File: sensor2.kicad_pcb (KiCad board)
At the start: 2 copper layers, 95 x 72 mm, 36 parts, among them CON1 DC2.5-9V, CON2 AVR-ISP-6, CON3 DM3AT-SF-PEJM5, IC1 ATMEGA328P-P, J1 AE-STEREO-MINI, P1 D-SUB9, P2 GMS6-CR6, P3 BATT, Q1 2SC1815, SW1 STOP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

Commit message: Developing
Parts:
- moved JP3 28.7 mm to (129.0, 129.0)
- moved CON3 26.0 mm to (104.0, 127.0)
- moved C3 25.8 mm to (117.1, 129.5)
- moved CON2 23.7 mm to (126.5, 136.4), turned to 0 degrees
- moved JP2 23.6 mm to (126.5, 129.0)
- moved J1 21.0 mm to (137.0, 133.0)
- moved JP1 18.6 mm to (124.0, 129.0)
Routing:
- net +3.3V: track 363.3 -> 265.4 mm
- net N-000005: track 92.3 -> 39.4 mm
- net N-000006: track 24.0 -> 0.00 mm
- net /3.3RX: track 11.6 -> 31.9 mm
- net /RX-LVTTL: track 55.8 -> 37.4 mm
- net /TX-LVTTL: track 50.8 -> 65.7 mm
- net N-0000022: track 2.54 -> 16.5 mm
- net N-000004: track 37.1 -> 26.2 mm
- net N-000003: track 40.5 -> 30.7 mm
- net GND: track 36.8 -> 27.1 mm
- net /3.3TX: track 13.7 -> 19.4 mm

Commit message: Critical miss
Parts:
- moved C3 16.1 mm to (101.0, 129.0)
- moved CON3 4.00 mm to (108.0, 127.0)
- moved R4 2.54 mm to (101.3, 111.0)
- moved P1 2.29 mm to (120.7, 108.0)
- moved P2 2.29 mm to (116.8, 111.0)
- moved CON2 2.18 mm to (125.2, 138.2), turned to 180 degrees
- moved R3 1.48 mm to (83.3, 111.3)
- moved R5 1.05 mm to (102.9, 108.2)
- moved R6 1.02 mm to (83.1, 106.9)
- moved CON1 1.00 mm to (68.0, 139.0)
- moved Q1 0.76 mm to (93.2, 106.9)
- moved U2 0.64 mm to (104.8, 119.4)
- moved SW1 0.51 mm to (134.6, 110.0)
- moved SW2 0.51 mm to (134.6, 118.1)
- moved C4 0.51 mm to (72.9, 106.4)
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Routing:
- net GND: track 27.1 -> 652.2 mm
- net +3.3V: track 265.4 -> 492.0 mm
- net N-000006: track 0.00 -> 108.9 mm
- net N-000004: track 26.2 -> 100.6 mm
- net N-000003: track 30.7 -> 99.6 mm, vias 0 -> 2
- net N-000002: track 0.00 -> 60.2 mm
- net /SDA: track 66.5 -> 121.4 mm
- net /SCL: track 69.2 -> 123.5 mm
- net N-0000022: track 16.5 -> 58.0 mm
- net N-000005: track 39.4 -> 0.00 mm
- net /3.3RX: track 31.9 -> 9.33 mm
- net +BATT: track 31.6 -> 49.3 mm
- net /TX-LVTTL: track 65.7 -> 82.7 mm
- net /RX-LVTTL: track 37.4 -> 33.9 mm
- net /TOGGLE: track 119.6 -> 121.8 mm
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- added copper zone on B.Cu, net GND
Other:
- net class Bold: via_dia 0.889 -> 1.524; via_drill 0.635 -> 1.016
- net class Default: via_dia 0.889 -> 1.524; via_drill 0.635 -> 1.016
- board text added: "JUMPER"

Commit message: First release
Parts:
- moved CON2 1.73 mm to (126.9, 137.7)
- moved R1 1.65 mm to (63.5, 126.6)
- moved R2 1.65 mm to (63.5, 129.2)
- moved R3 0.90 mm to (83.2, 110.4)
- moved R6 0.89 mm to (83.9, 106.9)
- moved JP1 0.76 mm to (124.7, 129.0)
- moved JP2 0.76 mm to (127.3, 129.0)
- moved JP3 0.76 mm to (129.8, 129.0)
- moved P2 0.38 mm to (116.8, 110.6)
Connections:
- CON1 pad 3: (no net) -> N-0000019
- P3 pad 2: GND -> N-0000019
- SW1 pad 3: (no net) -> GND
- SW2 pad 3: (no net) -> GND
- SW3 pad 4: (no net) -> GND
- SW4 pad 4: (no net) -> GND
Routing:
- net GND: track 652.2 -> 836.7 mm, vias 0 -> 4
- net N-000005: track 0.00 -> 63.9 mm, vias 0 -> 2
- net +3.3V: track 492.0 -> 532.8 mm
- net N-000006: track 99.6 -> 127.1 mm, vias 2 -> 4
- net N-0000019: track 0.00 -> 12.3 mm
- net +BATT: track 49.3 -> 39.7 mm
- net /SDA: track 121.4 -> 114.5 mm
- net /TOGGLE: track 121.8 -> 116.6 mm
- net /SCL: track 123.5 -> 119.8 mm
- net N-000007: track 108.9 -> 112.5 mm
- net /ADC0: track 33.0 -> 31.1 mm
- net N-000004: track 60.2 -> 58.7 mm
- net N-000001: track 100.6 -> 101.6 mm
- net N-000002: track 34.4 -> 35.2 mm
- net /3.3TX: track 18.8 -> 18.0 mm
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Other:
- board text added: "ISP"

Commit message: Developing
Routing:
- added copper zone on F.Cu, net GND
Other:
- net class Bold: via_dia 1.524 -> 0.889; via_drill 1.016 -> 0.635
- net class Default: via_dia 1.524 -> 0.889; via_drill 1.016 -> 0.635
- board text added: "Acc,Gyro"
- board text added: "Compass"
- board text added: "x"
- board text added: "y"
- board text added: "z"
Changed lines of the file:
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@@
-(kicad_pcb (version 3) (host pcbnew "(2013-07-07 BZR 4022)-stable")
+(kicad_pcb (version 3) (host pcbnew "(2013-jul-07)-stable")
   (general
     (links 97)
@@
     (area 32.57143 57.150001 152.2782 146.894321)
     (thickness 1.6)
-    (drawings 22)
+    (drawings 46)
     (tracks 676)
     (zones 0)
@@
     (last_trace_width 0.2032)
     (trace_clearance 0.2032)
-    (zone_clearance 0.4064)
+    (zone_clearance 0.508)
     (zone_45_only no)
     (trace_min 0.2032)
     (segment_width 0.2)
     (edge_width 0.1)
-    (via_size 1.524)
-    (via_drill 1.016)
+    (via_size 0.889)
+    (via_drill 0.635)
     (via_min_size 0.889)
     (via_min_drill 0.6096)
@@
     (visible_elements 7FFFFFFF)
     (pcbplotparams
-      (layerselection 283148289)
+      (layerselection 284196865)
       (usegerberextensions true)
       (excludeedgelayer true)
-      (linewidth 0.150000)
+      (linewidth 0.152400)
       (plotframeref false)
       (viasonmask true)
@@
     (clearance 0.2032)
     (trace_width 0.2032)
-    (via_dia 1.524)
-    (via_drill 1.016)
+    (via_dia 0.889)
+    (via_drill 0.635)
     (uvia_dia 0.508)
     (uvia_drill 0.127)
@@
     (clearance 0.2032)
     (trace_width 0.4064)
-    (via_dia 1.524)
-    (via_drill 1.016)
+    (via_dia 0.889)
+    (via_drill 0.635)
     (uvia_dia 0.508)
     (uvia_drill 0.127)
@@
     )
   )
+  (gr_text Compass (at 143.256 127.762) (layer F.SilkS)
+    (effects (font (size 1 1) (thickness 0.15)))
+  )
+  (gr_text z (at 140.716 125.984) (layer F.SilkS)
+    (effects (font (size 1.2 1.2) (thickness 0.15)))
+  )
+  (gr_text x (at 143.256 123.698) (layer F.SilkS)
+    (effects (font (size 1.2 1.2) (thickness 0.15)))
+  )
+  (gr_text y (at 144.78 125.984) (layer F.SilkS)
+    (effects (font (size 1.2 1.2) (thickness 0.15)))
+  )
+  (gr_circle (center 142.24 125.984) (end 142.748 126.492) (layer F.SilkS) (width 0.2))
+  (gr_line (start 142.748 126.492) (end 141.732 125.476) (angle 90) (layer F.SilkS) (width 0.2))
+  (gr_line (start 142.748 125.476) (end 141.732 126.492) (angle 90) (layer F.SilkS) (width 0.2))
+  (gr_line (start 144.018 125.984) (end 143.51 126.492) (angle 90) (layer F.SilkS) (width 0.2))
+  (gr_line (start 144.018 125.984) (end 143.51 125.476) (angle 90) (layer F.SilkS) (width 0.2))
+  (gr_line (start 142.24 124.206) (end 142.748 124.714) (angle 90) (layer F.SilkS) (width 0.2))
+  (gr_line (start 142.24 124.206) (end 141.732 124.714) (angle 90) (layer F.SilkS) (width 0.2))
+  (gr_line (start 142.24 125.984) (end 142.24 124.206) (angle 90) (layer F.SilkS) (width 0.2))
+  (gr_line (start 142.24 125.984) (end 144.018 125.984) (angle 90) (layer F.SilkS) (width 0.2))
+  (gr_text Acc,Gyro (at 134.874 127.762) (layer F.SilkS)
+    (effects (font (size 1 1) (thickness 0.15)))
+  )
+  (gr_text z (at 133.096 125.984) (layer F.SilkS)
+    (effects (font (size 1.2 1.2) (thickness 0.15)))
+  )
+  (gr_text y (at 135.636 123.698) (layer F.SilkS)
+    (effects (font (size 1.2 1.2) (thickness 0.15)))
+  )
+  (gr_text x (at 136.906 126.238) (layer F.SilkS)
+    (effects (font (size 1.2 1.2) (thickness 0.15)))
+  )
+  (gr_circle (center 134.366 125.984) (end 134.62 125.476) (layer F.SilkS) (width 0.2))
+  (gr_line (start 136.144 125.984) (end 135.636 126.492) (angle 90) (layer F.SilkS) (width 0.2))
+  (gr_line (start 136.144 125.984) (end 135.636 125.476) (angle 90) (layer F.SilkS) (width 0.2))
+  (gr_line (start 134.366 125.984) (end 136.144 125.984) (angle 90) (layer F.SilkS) (width 0.2))
+  (gr_line (start 134.366 124.206) (end 134.874 124.714) (angle 90) (layer F.SilkS) (width 0.2))
+  (gr_line (start 134.366 124.206) (end 133.858 124.714) (angle 90) (layer F.SilkS) (width 0.2))
+  (gr_line (start 134.366 125.984) (end 134.366 124.206) (angle 90) (layer F.SilkS) (width 0.2))
   (gr_text JUMPER (at 144.018 103.378) (layer F.SilkS)
     (effects (font (size 0.762 0.762) (thickness 0.1524)))
@@
       )
     )
+  )
+  (zone (net 16) (net_name GND) (layer F.Cu) (hatch edge 0.508)
+    (connect_pads (clearance 0.508))
+    (min_thickness 0.254)
+    (fill (arc_segments 16) (thermal_gap 0.508) (thermal_bridge_width 0.508))
+    (polygon
+      (pts
+        (xy 99 117) (xy 129 117) (xy 129 102) (xy 149 102) (xy 149 125)
+        (xy 125 125) (xy 122.5 122) (xy 110.5 122) (xy 110.5 125) (xy 107 125)
+        (xy 107 122) (xy 99 122)
+      )
+    )

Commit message: Release
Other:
- net class Bold: via_dia 0.889 -> 1.524; via_drill 0.635 -> 1.016
- net class Default: via_dia 0.889 -> 1.524; via_drill 0.635 -> 1.016
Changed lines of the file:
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@@
     (segment_width 0.2)
     (edge_width 0.1)
-    (via_size 0.889)
-    (via_drill 0.635)
+    (via_size 1.524)
+    (via_drill 1.016)
     (via_min_size 0.889)
     (via_min_drill 0.6096)
@@
       (drillshape 0)
       (scaleselection 1)
-      (outputdirectory garber/))
+      (outputdirectory gerber/))
   )
   (net 0 "")
@@
     (clearance 0.2032)
     (trace_width 0.2032)
-    (via_dia 0.889)
-    (via_drill 0.635)
+    (via_dia 1.524)
+    (via_drill 1.016)
     (uvia_dia 0.508)
     (uvia_drill 0.127)
@@
     (clearance 0.2032)
     (trace_width 0.4064)
-    (via_dia 0.889)
-    (via_drill 0.635)
+    (via_dia 1.524)
+    (via_drill 1.016)
     (uvia_dia 0.508)
     (uvia_drill 0.127)

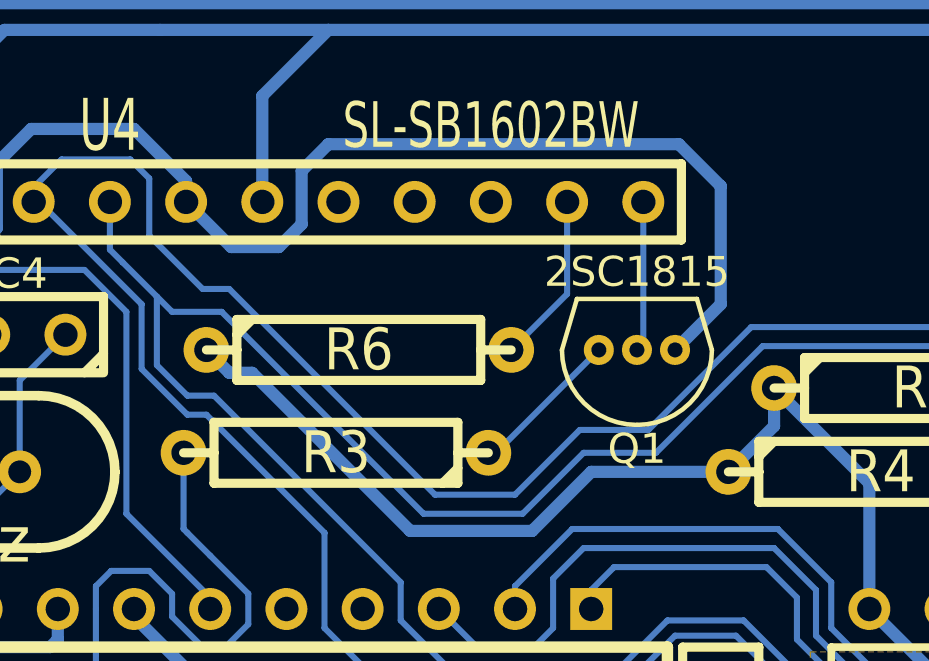
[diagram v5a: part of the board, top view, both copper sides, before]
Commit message: Modify Q1
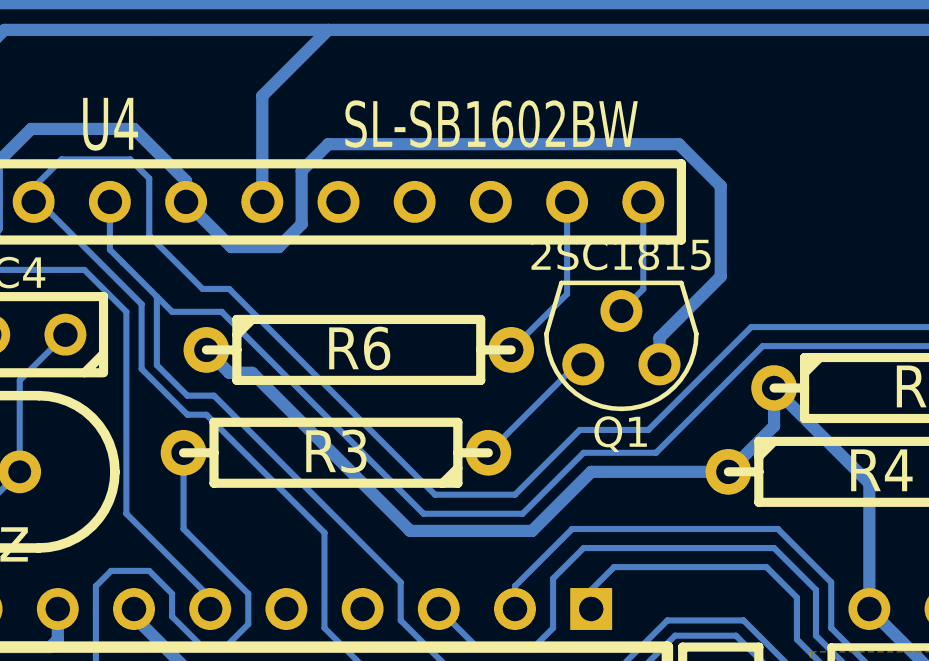
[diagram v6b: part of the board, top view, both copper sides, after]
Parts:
- Q1: footprint 2SC -> 2SC-2
- moved Q1 0.74 mm to (92.7, 106.4)
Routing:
- net N-000009: track 5.02 -> 3.94 mm
- net N-000003: track 5.10 -> 4.39 mm
- net GND: track 836.7 -> 837.4 mm
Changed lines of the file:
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@@
     (thickness 1.6)
     (drawings 46)
-    (tracks 676)
+    (tracks 677)
     (zones 0)
     (modules 36)
@@
     (last_trace_width 0.2032)
     (trace_clearance 0.2032)
-    (zone_clearance 0.508)
+    (zone_clearance 0.4064)
     (zone_45_only no)
     (trace_min 0.2032)
@@
       (viasonmask true)
       (mode 1)
-      (useauxorigin true)
+      (useauxorigin false)
       (hpglpennumber 1)
       (hpglpenspeed 20)
@@
       (psa4output false)
       (plotreference true)
-      (plotvalue true)
-      (plotothertext true)
+      (plotvalue false)
+      (plotothertext false)
       (plotinvisibletext false)
       (padsonsilk false)
@@
     )
   )
-  (module 2SC (layer F.Cu)
-    (at 93.218 106.934 180)
-    (fp_text reference Q1 (at 0 -3.3 180) (layer F.SilkS)
-      (effects (font (size 1 1) (thickness 0.15)))
-    )
-    (fp_text value 2SC1815 (at 0 2.6 180) (layer F.SilkS)
-      (effects (font (size 1 1) (thickness 0.15)))
-    )
-    (fp_line (start 2.5 0) (end 2 1.7) (layer F.SilkS) (width 0.15))
-    (fp_line (start 2 1.7) (end -2 1.7) (layer F.SilkS) (width 0.15))
-    (fp_line (start -2 1.7) (end -2.5 0) (layer F.SilkS) (width 0.15))
-    (fp_arc (start 0 0) (end 0 -2.5) (angle 90) (layer F.SilkS) (width 0.15))
-    (fp_arc (start 0 0) (end -2.5 0) (angle 90) (layer F.SilkS) (width 0.15))
-    (pad 3 thru_hole circle (at 0 0 180) (size 1 1) (drill 0.5)
-      (layers *.Cu *.Mask F.SilkS)
-      (net 29 N-000009)
-    )
-    (pad 2 thru_hole circle (at 1.27 0 180) (size 1 1) (drill 0.5)
-      (layers *.Cu *.Mask F.SilkS)
-      (net 21 N-000003)
-    )
-    (pad 1 thru_hole circle (at -1.27 0 180) (size 1 1) (drill 0.5)
-      (layers *.Cu *.Mask F.SilkS)
-      (net 16 GND)
-    )
-  )
   (module hole3-2mm (layer F.Cu)
     (at 58 75)
@@
     (pad "" np_thru_hole circle (at -4 -2.5 90) (size 1.3 1.3) (drill 1.3)
       (layers *.Cu *.Mask F.SilkS)
+    )
+  )
+  (module 2SC-2 (layer F.Cu)
+    (at 92.7 106.4 180)
+    (fp_text reference Q1 (at 0 -3.3 180) (layer F.SilkS)
+      (effects (font (size 1 1) (thickness 0.15)))
+    )
+    (fp_text value 2SC1815 (at 0 2.6 180) (layer F.SilkS)
+      (effects (font (size 1 1) (thickness 0.15)))
+    )
+    (fp_line (start 2.5 0) (end 2 1.7) (layer F.SilkS) (width 0.15))
+    (fp_line (start 2 1.7) (end -2 1.7) (layer F.SilkS) (width 0.15))
+    (fp_line (start -2 1.7) (end -2.5 0) (layer F.SilkS) (width 0.15))
+    (fp_arc (start 0 0) (end 0 -2.5) (angle 90) (layer F.SilkS) (width 0.15))
+    (fp_arc (start 0 0) (end -2.5 0) (angle 90) (layer F.SilkS) (width 0.15))
+    (pad 3 thru_hole circle (at 0 0.762 180) (size 1.4 1.4) (drill 0.8)
+      (layers *.Cu *.Mask F.SilkS)
+      (net 29 N-000009)
+    )
+    (pad 2 thru_hole circle (at 1.27 -1.016 180) (size 1.4 1.4) (drill 0.8)
+      (layers *.Cu *.Mask F.SilkS)
+      (net 21 N-000003)
+    )
+    (pad 1 thru_hole circle (at -1.27 -1.016 180) (size 1.4 1.4) (drill 0.8)
+      (layers *.Cu *.Mask F.SilkS)
+      (net 16 GND)
     )
   )
@@
   (segment (start 120.015 118.745) (end 126.492 118.745) (width 0.2032) (layer B.Cu) (net 15))
   (segment (start 120.015 118.745) (end 102.235 118.745) (width 0.2032) (layer B.Cu) (net 15))
+  (segment (start 96.012 101.473) (end 96.012 104.488) (width 0.4064) (layer B.Cu) (net 16))
+  (segment (start 96.012 101.473) (end 94.615 100.076) (width 0.4064) (layer B.Cu) (net 16))
+  (segment (start 94.615 100.076) (end 82.931 100.076) (width 0.4064) (layer B.Cu) (net 16))
+  (segment (start 82.931 100.076) (end 82.042 100.965) (width 0.4064) (layer B.Cu) (net 16))
+  (segment (start 82.042 100.965) (end 82.042 102.743) (width 0.4064) (layer B.Cu) (net 16))
+  (segment (start 82.042 102.743) (end 81.28 103.505) (width 0.4064) (layer B.Cu) (net 16))
+  (segment (start 81.28 103.505) (end 79.695 103.505) (width 0.4064) (layer B.Cu) (net 16))
+  (segment (start 78.19 102) (end 79.695 103.505) (width 0.4064) (layer B.Cu) (net 16))
+  (segment (start 93.97 106.53) (end 93.97 107.416) (width 0.4064) (layer B.Cu) (net 16))
+  (segment (start 96.012 104.488) (end 93.97 106.53) (width 0.4064) (layer B.Cu) (net 16))
   (segment (start 79.502 128.016) (end 87.122 135.636) (width 0.4064) (layer F.Cu) (net 16))
   (segment (start 87.122 135.636) (end 87.122 140.716) (width 0.4064) (layer F.Cu) (net 16))
@@
   (segment (start 121.666 126.619) (end 121.666 123.19) (width 0.4064) (layer B.Cu) (net 16))
   (segment (start 121.158 127.127) (end 121.666 126.619) (width 0.4064) (layer B.Cu) (net 16))
-  (segment (start 94.488 106.934) (end 96.012 105.41) (width 0.4064) (layer B.Cu) (net 16))
-  (segment (start 79.695 103.505) (end 78.19 102) (width 0.4064) (layer B.Cu) (net 16))
-  (segment (start 81.28 103.505) (end 79.695 103.505) (width 0.4064) (layer B.Cu) (net 16))
-  (segment (start 82.042 102.743) (end 81.28 103.505) (width 0.4064) (layer B.Cu) (net 16))
-  (segment (start 82.042 100.965) (end 82.042 102.743) (width 0.4064) (layer B.Cu) (net 16))
-  (segment (start 82.931 100.076) (end 82.042 100.965) (width 0.4064) (layer B.Cu) (net 16))
-  (segment (start 94.615 100.076) (end 82.931 100.076) (width 0.4064) (layer B.Cu) (net 16))
-  (segment (start 96.012 101.473) (end 94.615 100.076) (width 0.4064) (layer B.Cu) (net 16))
-  (segment (start 96.012 105.41) (end 96.012 101.473) (width 0.4064) (layer B.Cu) (net 16))
   (segment (start 108.585 123.19) (end 108.585 121.92) (width 0.4064) (layer B.Cu) (net 16))
   (segment (start 108.585 121.92) (end 107.569 120.904) (width 0.4064) (layer B.Cu) (net 16))
@@
   (segment (start 129.794 127.254) (end 127.762 125.222) (width 0.2032) (layer B.Cu) (net 20))
   (segment (start 129.794 127.762) (end 127.254 127.762) (width 0.2032) (layer B.Cu) (net 20) (status 20))
-  (segment (start 91.948 106.934) (end 88.519 110.363) (width 0.2032) (layer B.Cu) (net 21))
-  (segment (start 88.519 110.363) (end 88.265 110.363) (width 0.2032) (layer B.Cu) (net 21))
+  (segment (start 91.43 107.416) (end 91.212 107.416) (width 0.2032) (layer B.Cu) (net 21) (status C00000))
+  (segment (start 91.212 107.416) (end 88.265 110.363) (width 0.2032) (layer B.Cu) (net 21) (status C00000))
   (segment (start 123.063 132.588) (end 124.333 133.858) (width 0.2032) (layer B.Cu) (net 22))
   (segment (start 123.063 132.588) (end 123.063 127) (width 0.2032) (layer B.Cu) (net 22))
@@
   (segment (start 90.89 102) (end 90.89 105.071) (width 0.2032) (layer B.Cu) (net 28))
   (segment (start 90.89 105.071) (end 89.027 106.934) (width 0.2032) (layer B.Cu) (net 28))
-  (segment (start 93.43 102) (end 93.43 106.722) (width 0.2032) (layer B.Cu) (net 29))
-  (segment (start 93.43 106.722) (end 93.218 106.934) (width 0.2032) (layer B.Cu) (net 29))
+  (segment (start 93.43 102) (end 93.43 104.908) (width 0.2032) (layer B.Cu) (net 29))
+  (segment (start 93.43 104.908) (end 92.7 105.638) (width 0.2032) (layer B.Cu) (net 29))
   (zone (net 16) (net_name GND) (layer B.Cu) (hatch edge 0.508)
     (connect_pads (clearance 0.4064))

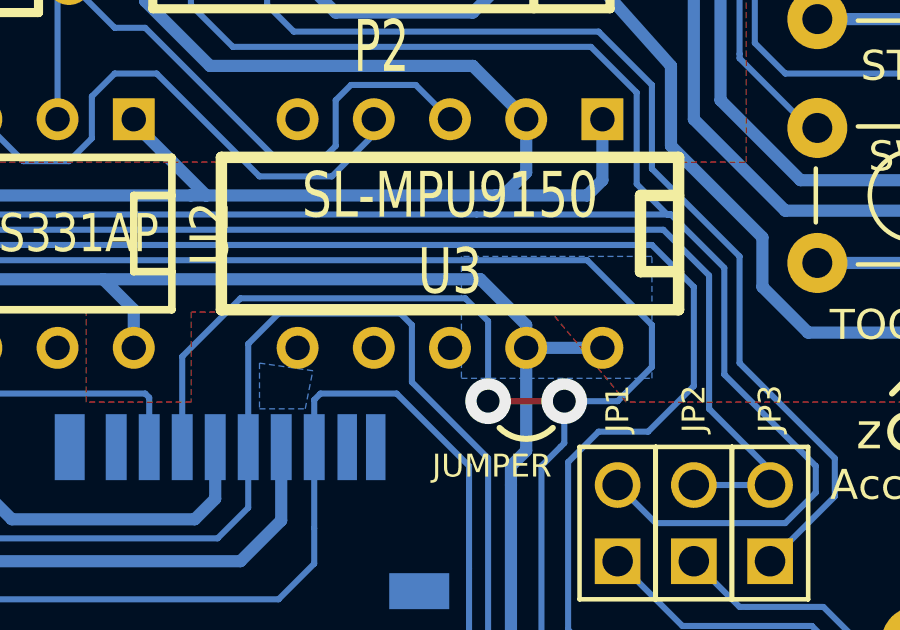
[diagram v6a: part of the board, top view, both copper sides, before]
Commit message: Connect FSYNC pin to GND
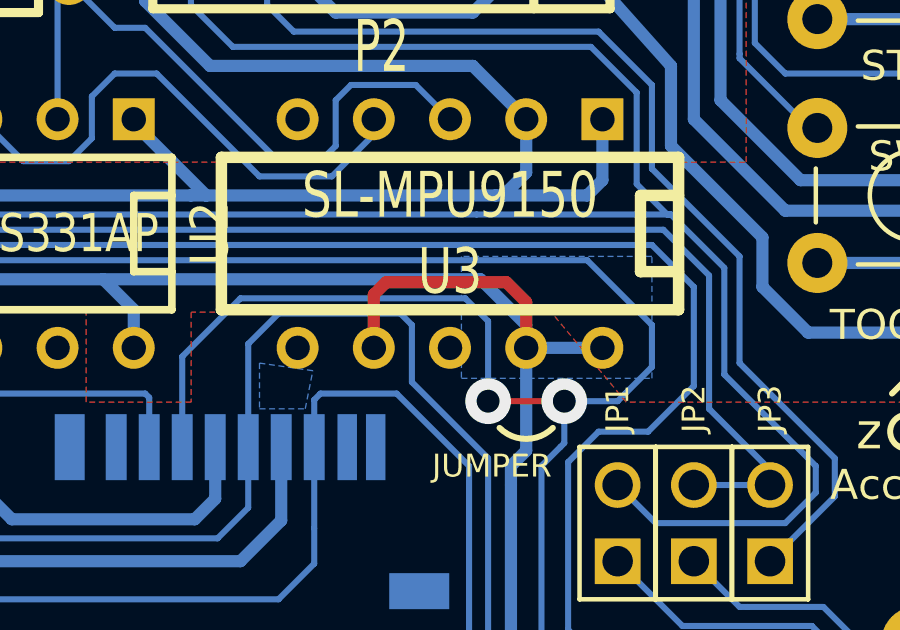
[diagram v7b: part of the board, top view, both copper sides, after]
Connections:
- U3 pad 7: (no net) -> GND
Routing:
- net GND: track 837.4 -> 846.2 mm
